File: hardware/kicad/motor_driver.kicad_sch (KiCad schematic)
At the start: 0 parts

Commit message: feat: added reverse polarity protection
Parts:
- added C1: 0.1uF, symbol Device:C
- added C2: 470uF, symbol Device:C_Polarized
- added J1: FROM_MCU, Connector_PinHeader_2.54mm:PinHeader_1x04_P2.54mm_Vertical, symbol PCM_SparkFun-Connector:Conn_01x04_P2.54mm_Header_Horizontal_SMD
- added J2: TO_MOTOR, Connector_JST:JST_XH_B5B-XH-A_1x05_P2.50mm_Vertical, symbol Connector:Conn_01x05_Pin
- added J3: 5V_IN, Connector_PinHeader_2.54mm:PinHeader_1x02_P2.54mm_Vertical, symbol Connector:Conn_01x02_Pin
- added J4: PRT-10811, PRT-10811_SPK, symbol Power Jack:PRT-10811
- added Q1, Q2: IRLML6402, Package_TO_SOT_SMD:SOT-23, symbol Transistor_FET:IRLML6402
- added R1, R2, R3, R4: 1.5k, symbol Device:R
- added R12, R5, R6, R7, R8, R9: 100k, symbol Device:R
- added U1: ULN2003A, Package_DIP:DIP-16_W7.62mm, symbol Transistor_Array:ULN2003A
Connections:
- new net: C1.1, C2.1, J2.1 (Pin_1), Q1.3 (D), Q2.3 (D), U1.9 (COM)
- new net: C1.2, C2.2, U1.8 (GND)
- new net: J4.2, J4.3, R12.1
- new net: Q1.1 (G), R12.2
- new net: J2.2 (Pin_2), U1.16 (O1)
- new net: J2.3 (Pin_3), U1.15 (O2)
- new net: J2.4 (Pin_4), U1.14 (O3)
- new net: J2.5 (Pin_5), U1.13 (O4)
- new net: J4.1, Q1.2 (S)
- new net: J1.1 (Pin_1), R4.1
- new net: R4.2, R5.2, U1.4 (I4)
- new net: J1.2 (Pin_2), R3.1
- new net: J1.3 (Pin_3), R2.1
- new net: J1.4 (Pin_4), R1.1
- new net: R5.1, R6.1, R7.1, R8.1
- new net: R1.2, R8.2, U1.1 (I1)
- new net: J3.1 (Pin_1), Q2.2 (S)
- new net: J3.2 (Pin_2), R9.1
- new net: R2.2, R7.2, U1.2 (I2)
- new net: R3.2, R6.2, U1.3 (I3)
- new net: Q2.1 (G), R9.2
- no-connect marks 0 -> 6

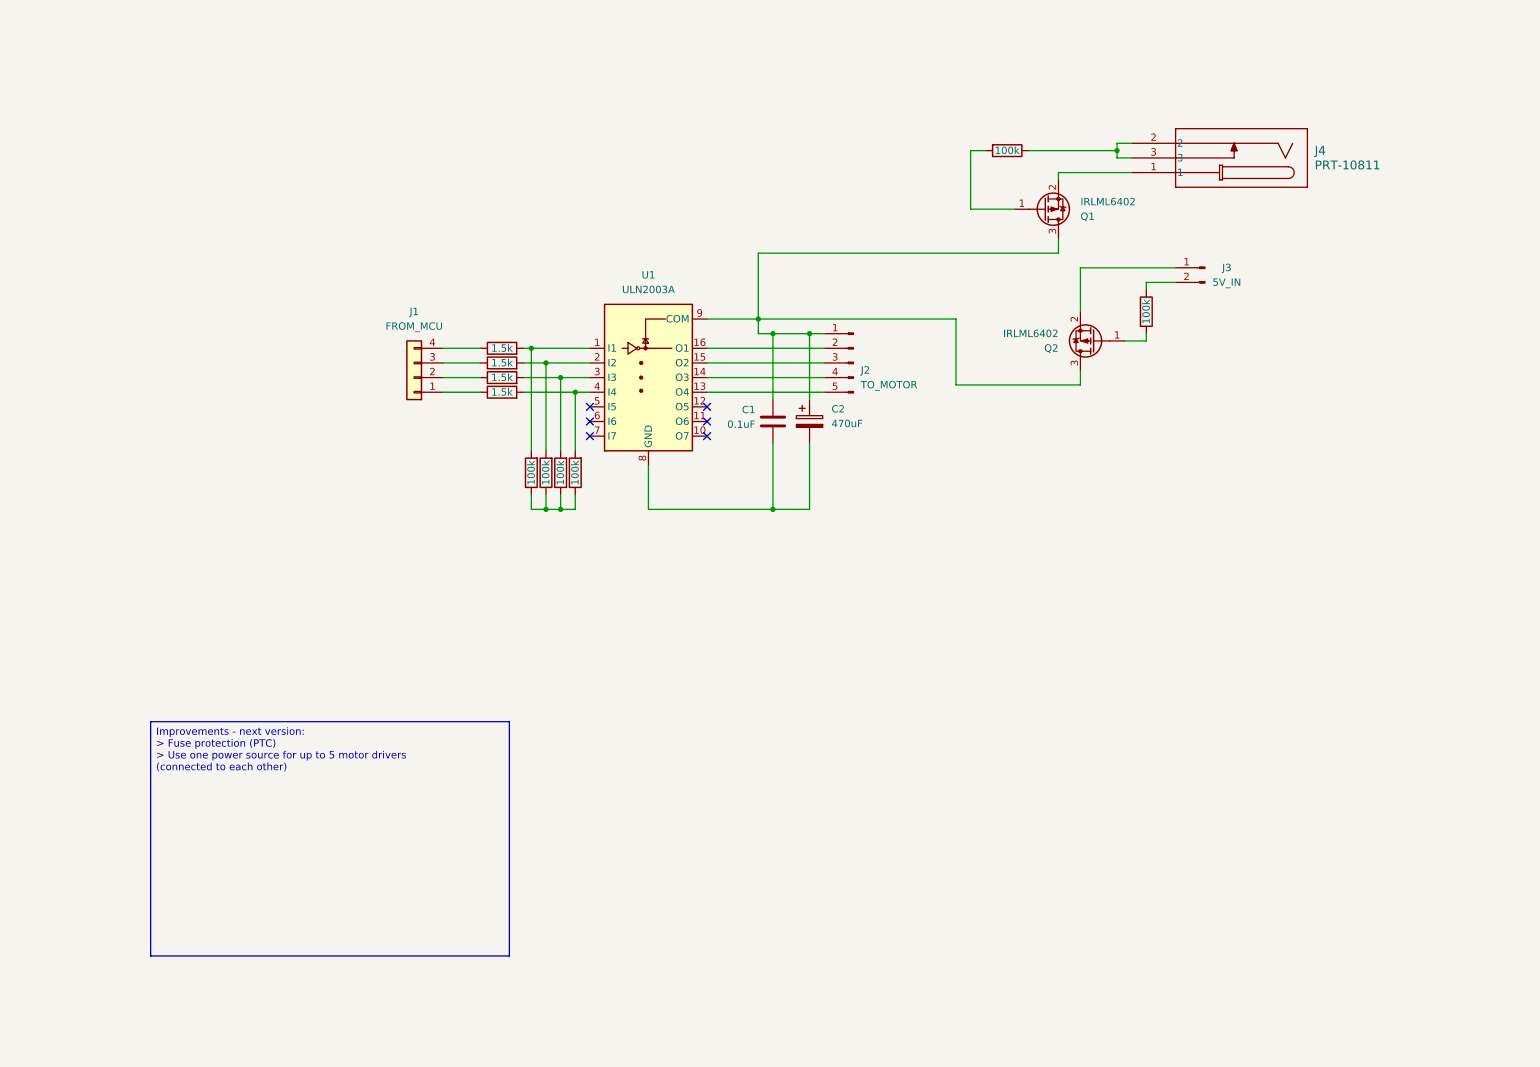
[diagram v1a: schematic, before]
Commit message: perf: changed mosfet to diodes - polarity protection
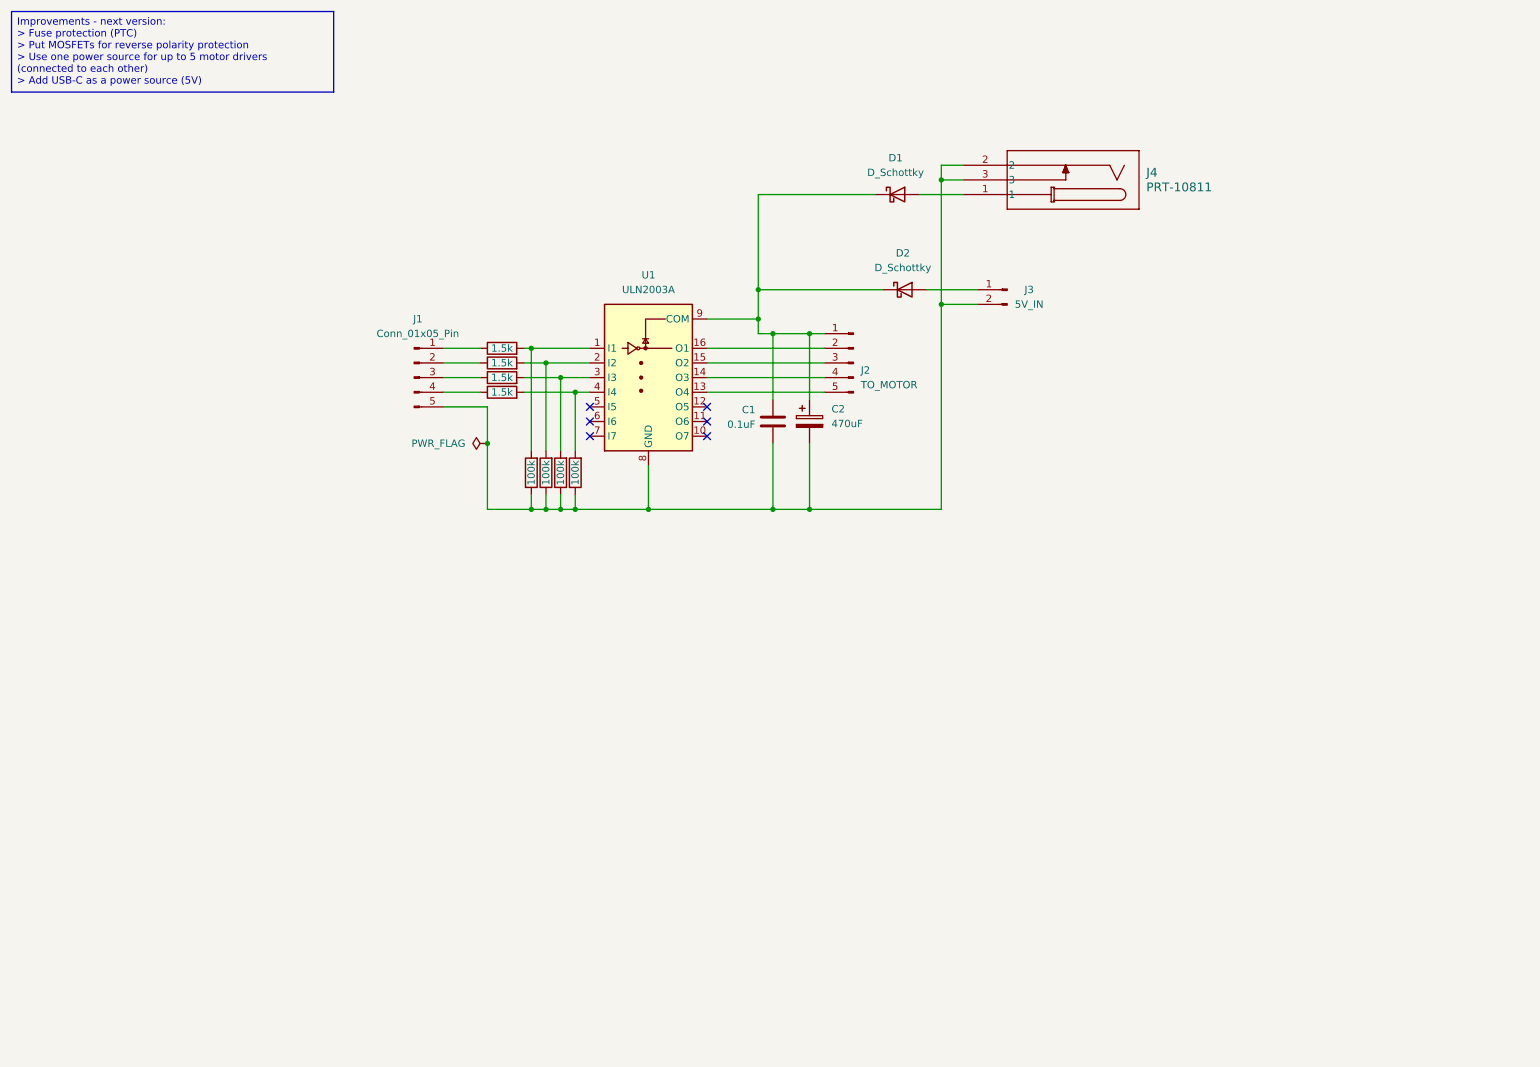
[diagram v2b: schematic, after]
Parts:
- removed J1: FROM_MCU, Connector_PinHeader_2.54mm:PinHeader_1x04_P2.54mm_Vertical, symbol PCM_SparkFun-Connector:Conn_01x04_P2.54mm_Header_Horizontal_SMD
- removed Q1, Q2: IRLML6402, Package_TO_SOT_SMD:SOT-23, symbol Transistor_FET:IRLML6402
- removed R12, R9: 100k, symbol Device:R
- added D1, D2: D_Schottky, symbol Device:D_Schottky
- added J1: Conn_01x05_Pin, Connector_PinHeader_2.54mm:PinHeader_1x05_P2.54mm_Vertical, symbol Connector:Conn_01x05_Pin
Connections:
- net at C1.1, C2.1, J2.1 (Pin_1)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: now also D1.1 (K), D2.1 (K)
- net at C1.2, C2.2, U1.8 (GND): now also J3.2 (Pin_2), J4.2, J4.3, R5.1, R6.1, R7.1, R8.1, J1.5 (Pin_5)
- net at J4.1: now also D1.2 (A)
- net at R4.1: now also J1.4 (Pin_4)
- net at R3.1: now also J1.3 (Pin_3)
- net at R2.1: now also J1.2 (Pin_2)
- net at R1.1: now also J1.1 (Pin_1)
- net at J3.1 (Pin_1): now also D2.2 (A)
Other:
- moved on the sheet: J3, J4

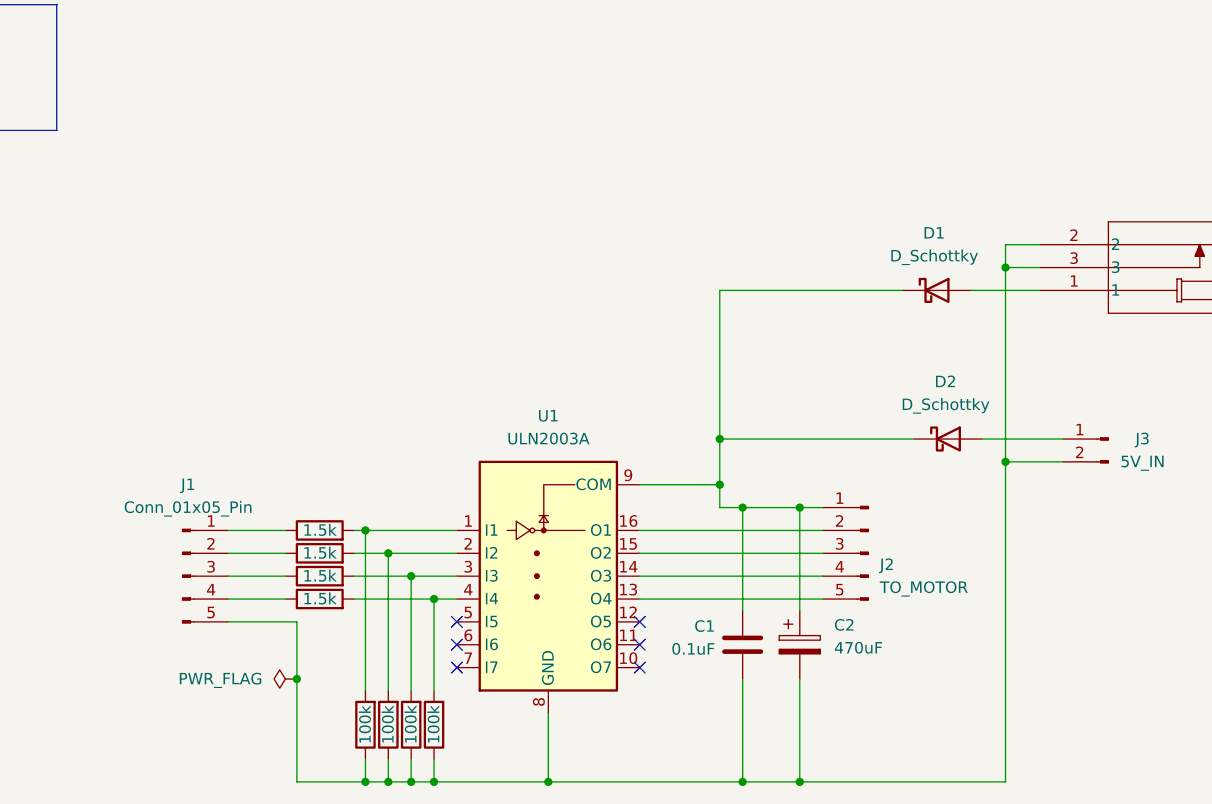
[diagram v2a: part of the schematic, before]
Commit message: feat: schematic to simulation circuit - not yet simulated
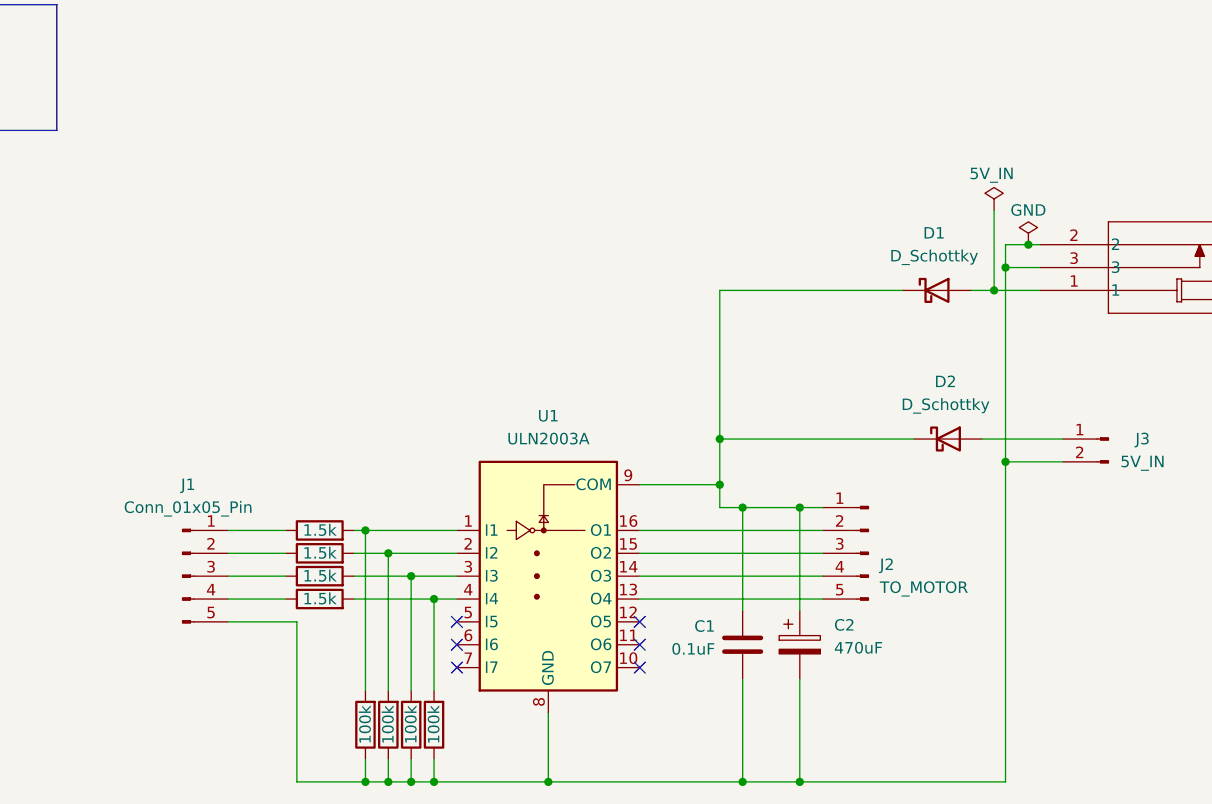
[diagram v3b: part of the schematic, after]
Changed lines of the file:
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@@
+	)
+	(junction
+		(at 179.07 40.64)
+		(diameter 0)
+		(color 0 0 0 0)
 	)
 	(junction
@@
 	)
 	(junction
-		(at 97.79 88.9)
-		(diameter 0)
-		(color 0 0 0 0)
-	)
-	(junction
 		(at 144.78 67.31)
 		(diameter 0)
@@
 	)
 	(junction
+		(at 175.26 45.72)
+		(diameter 0)
+		(color 0 0 0 0)
+	)
+	(junction
 		(at 147.32 100.33)
 		(diameter 0)
@@
 	(wire
 		(pts
-			(xy 180.34 40.64) (xy 176.53 40.64)
+			(xy 180.34 40.64) (xy 179.07 40.64)
 		)
 		(stroke
@@
 	(wire
 		(pts
-			(xy 97.79 88.9) (xy 97.79 100.33)
+			(xy 97.79 82.55) (xy 97.79 100.33)
 		)
 		(stroke
@@
 	(wire
 		(pts
-			(xy 97.79 82.55) (xy 97.79 88.9)
-		)
-		(stroke
-			(width 0)
-			(type default)
-		)
-	)
-	(wire
-		(pts
 			(xy 144.78 62.23) (xy 144.78 67.31)
 		)
@@
 	(wire
 		(pts
+			(xy 179.07 40.64) (xy 176.53 40.64)
+		)
+		(stroke
+			(width 0)
+			(type default)
+		)
+	)
+	(wire
+		(pts
 			(xy 144.78 45.72) (xy 144.78 62.23)
 		)
@@
 	(wire
 		(pts
-			(xy 172.72 45.72) (xy 180.34 45.72)
+			(xy 175.26 36.83) (xy 175.26 45.72)
+		)
+		(stroke
+			(width 0)
+			(type default)
+		)
+	)
+	(wire
+		(pts
+			(xy 172.72 45.72) (xy 175.26 45.72)
 		)
 		(stroke
@@
 		(pts
 			(xy 165.1 45.72) (xy 144.78 45.72)
+		)
+		(stroke
+			(width 0)
+			(type default)
+		)
+	)
+	(wire
+		(pts
+			(xy 175.26 45.72) (xy 180.34 45.72)
 		)
 		(stroke
@@
 	)
 	(symbol
+		(lib_id "power:PWR_FLAG")
+		(at 179.07 40.64 0)
+		(unit 1)
+		(exclude_from_sim no)
+		(in_bom yes)
+		(on_board yes)
+		(dnp no)
+		(property "Reference" "#FLG02"
+			(at 179.07 38.735 0)
+			(effects
+				(font
+					(size 1.27 1.27)
+				)
+				(hide yes)
+			)
+		)
+		(property "Value" "GND"
+			(at 179.07 36.83 0)
+			(effects
+				(font
+					(size 1.27 1.27)
+				)
+			)
+		)
+		(property "Footprint" ""
+			(at 179.07 40.64 0)
+			(effects
+				(font
+					(size 1.27 1.27)
+				)
+				(hide yes)
+			)
+		)
+		(property "Datasheet" "~"
+			(at 179.07 40.64 0)
+			(effects
+				(font
+					(size 1.27 1.27)
+				)
+				(hide yes)
+			)
+		)
+		(property "Description" "Special symbol for telling ERC where power comes from"
+			(at 179.07 40.64 0)
+			(effects
+				(font
+					(size 1.27 1.27)
+				)
+				(hide yes)
+			)
+		)
+		(pin "1"
+		)
+		(instances
+			(project ""
+				(path "/b7a12314-1361-4fdf-a1f9-9f4ac4cac78f"
+					(reference "#FLG02")
+					(unit 1)
+				)
+			)
+		)
+	)
+	(symbol
 		(lib_id "Device:R")
 		(at 105.41 93.98 180)
@@
 	)
 	(symbol
+		(lib_id "power:PWR_FLAG")
+		(at 175.26 36.83 0)
+		(unit 1)
+		(exclude_from_sim no)
+		(in_bom yes)
+		(on_board yes)
+		(dnp no)
+		(property "Reference" "#FLG01"
+			(at 175.26 34.925 0)
+			(effects
+				(font
+					(size 1.27 1.27)
+				)
+				(hide yes)
+			)
+		)
+		(property "Value" "5V_IN"
+			(at 175.006 32.766 0)
+			(effects
+				(font
+					(size 1.27 1.27)
+				)
+			)
+		)
+		(property "Footprint" ""
+			(at 175.26 36.83 0)
+			(effects
+				(font
+					(size 1.27 1.27)
+				)
+				(hide yes)
+			)
+		)
+		(property "Datasheet" "~"
+			(at 175.26 36.83 0)
+			(effects
+				(font
+					(size 1.27 1.27)
+				)
+				(hide yes)
+			)
+		)
+		(property "Description" "Special symbol for telling ERC where power comes from"
+			(at 175.26 36.83 0)
+			(effects
+				(font
+					(size 1.27 1.27)
+				)
+				(hide yes)
+			)
+		)
+		(pin "1"
+		)
+		(instances
+			(project ""
+				(path "/b7a12314-1361-4fdf-a1f9-9f4ac4cac78f"
+					(reference "#FLG01")
+					(unit 1)
+				)
+			)
+		)
+	)
+	(symbol
 		(lib_id "Device:R")
 		(at 100.33 77.47 90)
@@
 					(unit 1)
 				)
-			)
-		)
-	)
-	(symbol
-		(lib_id "power:PWR_FLAG")
-		(at 97.79 88.9 90)
-		(unit 1)
-		(exclude_from_sim no)
-		(in_bom yes)
-		(on_board yes)
-		(dnp no)
-		(fields_autoplaced yes)
-		(property "Reference" "#FLG01"
-			(at 95.885 88.9 0)
-			(effects
-				(font
-					(size 1.27 1.27)
-				)
-				(hide yes)
-			)
-		)
-		(property "Value" "PWR_FLAG"
-			(at 93.98 88.8999 90)
-			(effects
-				(font
-					(size 1.27 1.27)
-				)
-				(justify left)
-			)
-		)
-		(property "Footprint" ""
-			(at 97.79 88.9 0)
-			(effects
-				(font
-					(size 1.27 1.27)
-				)
-				(hide yes)
-			)
-		)
-		(property "Datasheet" "~"
-			(at 97.79 88.9 0)
-			(effects
-				(font
-					(size 1.27 1.27)
-				)
-				(hide yes)
-			)
-		)
-		(property "Description" "Special symbol for telling ERC where power comes from"
-			(at 97.79 88.9 0)
-			(effects
-				(font
-					(size 1.27 1.27)
-				)
-				(hide yes)
-			)
-		)
-		(pin "1"
-		)
-		(instances
-			(project ""
-				(path "/b7a12314-1361-4fdf-a1f9-9f4ac4cac78f"
-					(reference "#FLG01")
-					(unit 1)
-				)
